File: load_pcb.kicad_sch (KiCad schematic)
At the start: 32 parts, among them J1 Conn_01x16, J2 Conn_01x08, J3 Conn_01x10, P1 282837-2, P2 282837-2, P3 282837-2, P4 282837-2, Q1 BC846BPDW1, Q2 IRFP064V, Q3 IRFP064V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

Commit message: Changed positions of connectors
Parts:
- R14, R15, R16, R17: footprint Resistor_SMD:R_MiniMELF_MMA-0204 -> Resistor_THT:R_Axial_DIN0207_L6.3mm_D2.5mm_P10.16mm_Horizontal
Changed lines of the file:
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@@
       (effects (font (size 1.27 1.27)) (justify left))
     )
-    (property "Footprint" "Resistor_SMD:R_MiniMELF_MMA-0204" (id 2) (at 236.982 77.47 90)
+    (property "Footprint" "Resistor_THT:R_Axial_DIN0207_L6.3mm_D2.5mm_P10.16mm_Horizontal" (id 2) (at 236.982 77.47 90)
       (effects (font (size 1.27 1.27)) hide)
     )
@@
       (effects (font (size 1.27 1.27)) (justify left))
     )
-    (property "Footprint" "Resistor_SMD:R_MiniMELF_MMA-0204" (id 2) (at 248.412 121.92 90)
+    (property "Footprint" "Resistor_THT:R_Axial_DIN0207_L6.3mm_D2.5mm_P10.16mm_Horizontal" (id 2) (at 248.412 121.92 90)
       (effects (font (size 1.27 1.27)) hide)
     )
@@
       (effects (font (size 1.27 1.27)) (justify left))
     )
-    (property "Footprint" "Resistor_SMD:R_MiniMELF_MMA-0204" (id 2) (at 236.982 90.17 90)
+    (property "Footprint" "Resistor_THT:R_Axial_DIN0207_L6.3mm_D2.5mm_P10.16mm_Horizontal" (id 2) (at 236.982 90.17 90)
       (effects (font (size 1.27 1.27)) hide)
     )
@@
       (effects (font (size 1.27 1.27)) (justify left))
     )
-    (property "Footprint" "Resistor_SMD:R_MiniMELF_MMA-0204" (id 2) (at 248.412 109.22 90)
+    (property "Footprint" "Resistor_THT:R_Axial_DIN0207_L6.3mm_D2.5mm_P10.16mm_Horizontal" (id 2) (at 248.412 109.22 90)
       (effects (font (size 1.27 1.27)) hide)
     )
@@
     )
     (path "/4ef2169a-f28b-4852-977e-0f0ba8408b95"
-      (reference "R14") (unit 1) (value "62k") (footprint "Resistor_SMD:R_MiniMELF_MMA-0204")
+      (reference "R14") (unit 1) (value "62k") (footprint "Resistor_THT:R_Axial_DIN0207_L6.3mm_D2.5mm_P10.16mm_Horizontal")
     )
     (path "/809e2eb5-7286-4453-bbbc-874b30752de5"
-      (reference "R15") (unit 1) (value "62k") (footprint "Resistor_SMD:R_MiniMELF_MMA-0204")
+      (reference "R15") (unit 1) (value "62k") (footprint "Resistor_THT:R_Axial_DIN0207_L6.3mm_D2.5mm_P10.16mm_Horizontal")
     )
     (path "/87e237c7-673a-475b-aae1-645c481bc5fe"
-      (reference "R16") (unit 1) (value "62k") (footprint "Resistor_SMD:R_MiniMELF_MMA-0204")
+      (reference "R16") (unit 1) (value "62k") (footprint "Resistor_THT:R_Axial_DIN0207_L6.3mm_D2.5mm_P10.16mm_Horizontal")
     )
     (path "/5b2c9207-c2da-4144-981f-da5833109a74"
-      (reference "R17") (unit 1) (value "62k") (footprint "Resistor_SMD:R_MiniMELF_MMA-0204")
+      (reference "R17") (unit 1) (value "62k") (footprint "Resistor_THT:R_Axial_DIN0207_L6.3mm_D2.5mm_P10.16mm_Horizontal")
     )
     (path "/08372d8d-6e01-436e-bce7-15647a9603ce"

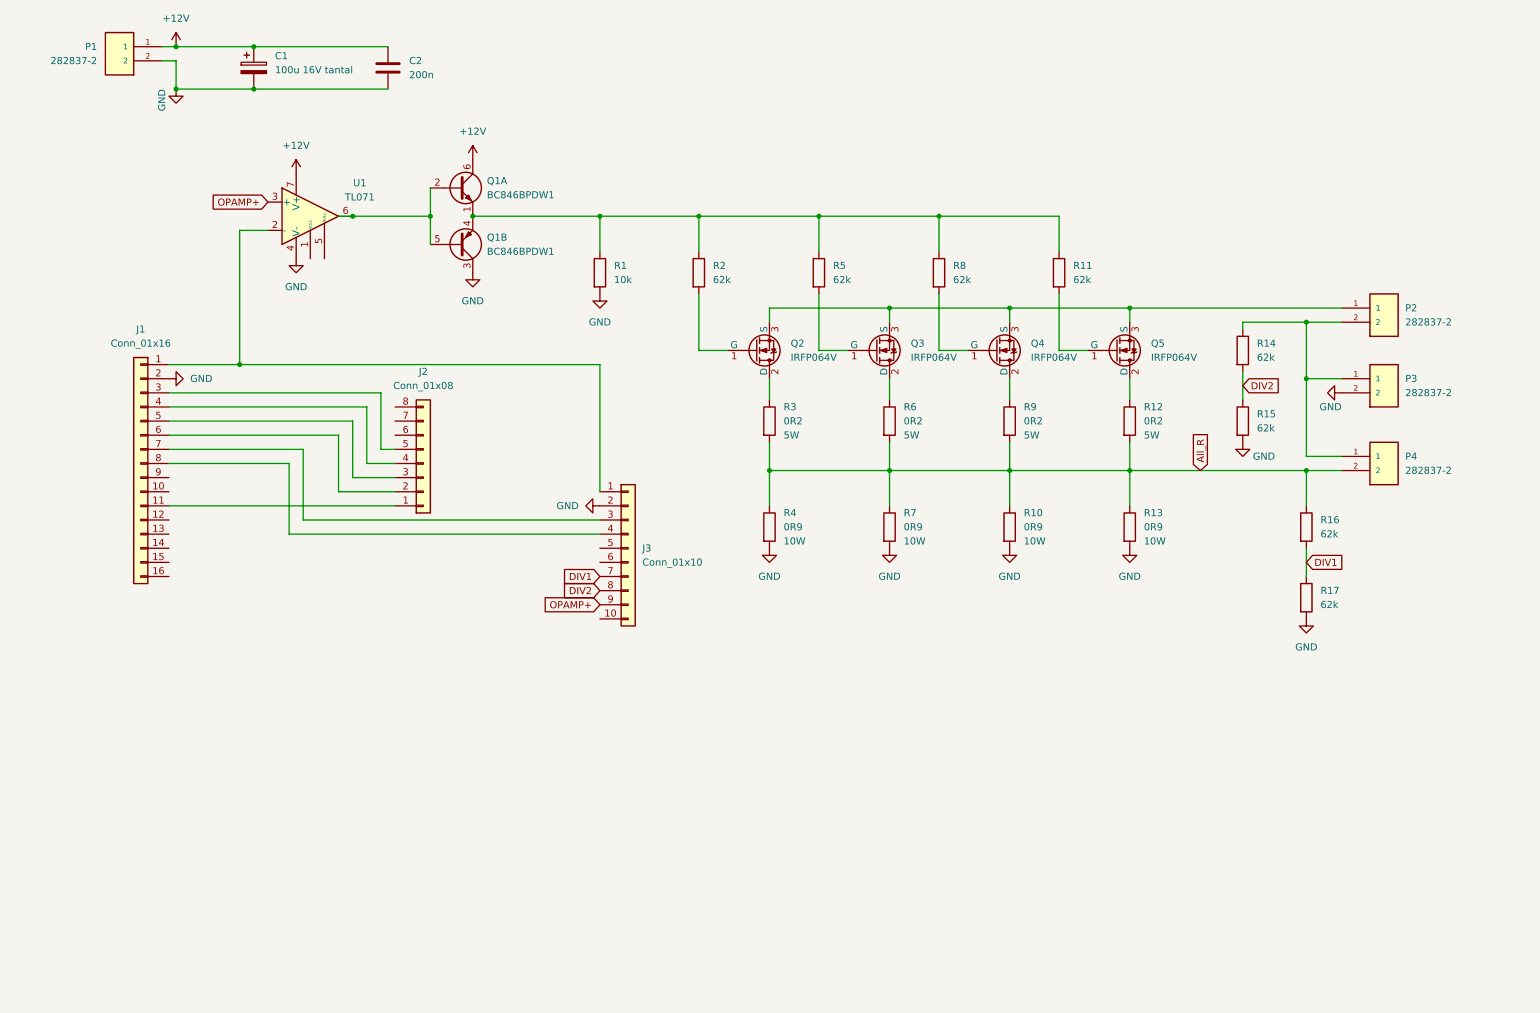
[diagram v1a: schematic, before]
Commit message: Added DAC and corrected positions of SMD/THD
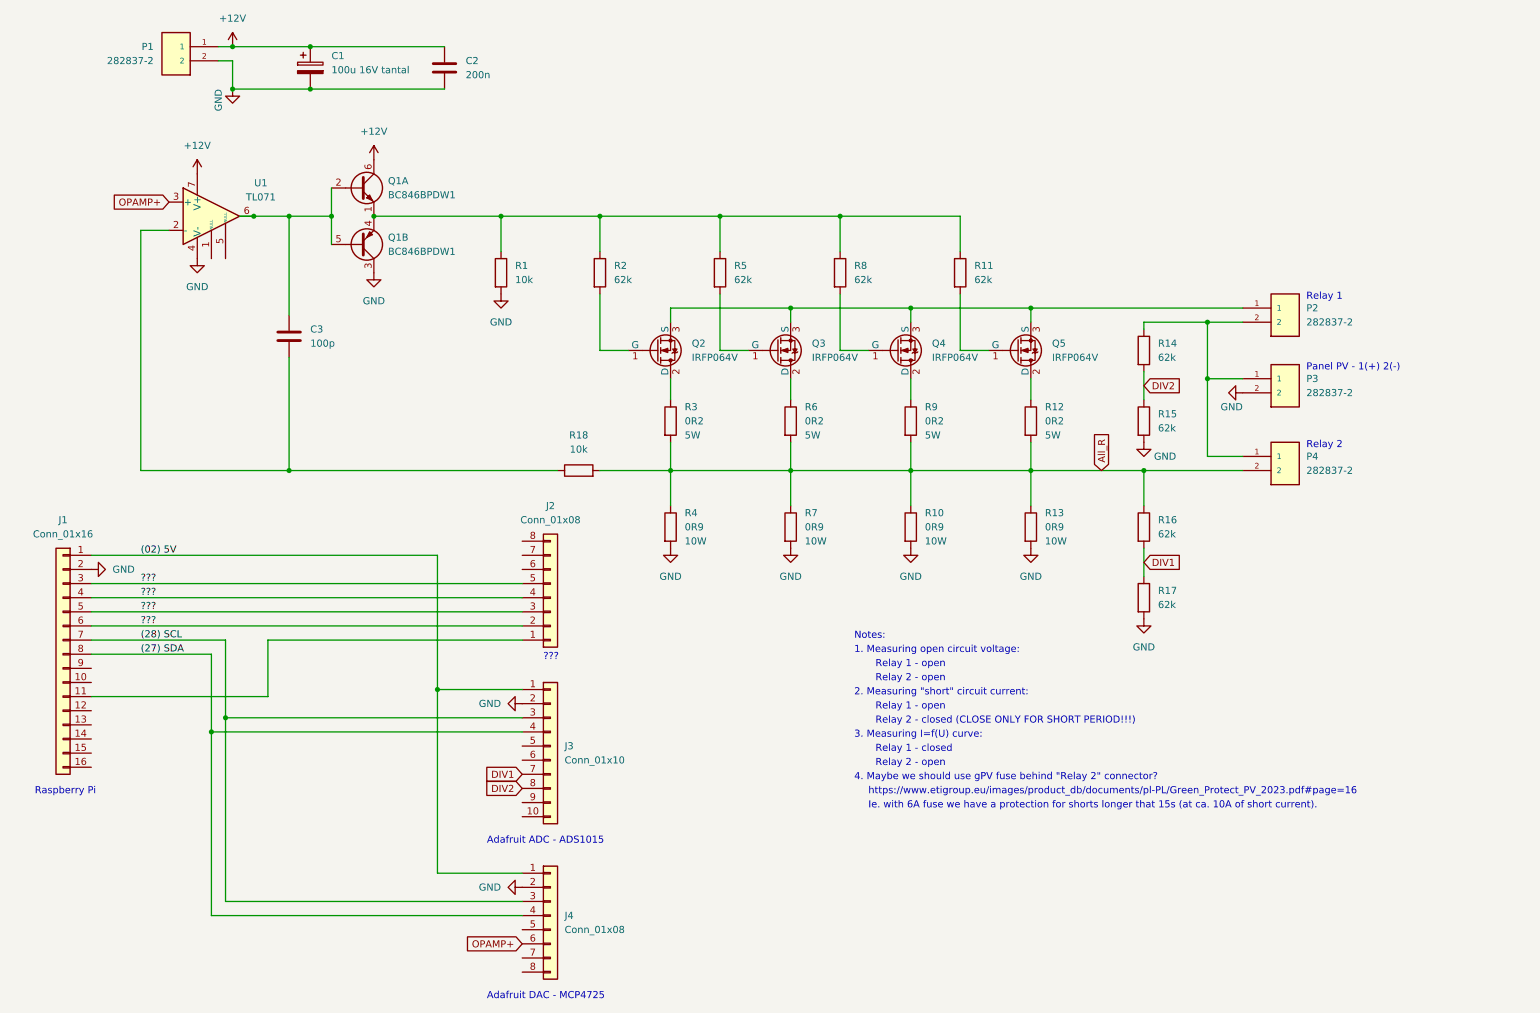
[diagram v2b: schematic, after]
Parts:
- added C3: 100p, Capacitor_SMD:C_1206_3216Metric_Pad1.33x1.80mm_HandSolder, symbol Device:C
- added J4: Conn_01x08, Connector_PinSocket_2.54mm:PinSocket_1x08_P2.54mm_Vertical, symbol Connector_Generic:Conn_01x08
- added R18: 10k, Resistor_SMD:R_1206_3216Metric_Pad1.30x1.75mm_HandSolder, symbol Device:R
- R1, R11, R2, R5, R8: footprint Resistor_SMD:R_MiniMELF_MMA-0204 -> Resistor_SMD:R_1206_3216Metric_Pad1.30x1.75mm_HandSolder
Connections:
- net All_R: now also R18.2
- net GND: now also J4.2 (Pin_2)
- net OPAMP+: now also J4.6 (Pin_6); no longer J3.9 (Pin_9)
- net (02) 5V: now reaches J1.1 (Pin_1), J3.1 (Pin_1)
- net (02) 5V: now also J4.1 (Pin_1); no longer U1.2 (-)
- net at Q1.2 (B1), Q1.5 (B2), U1.6: now also C3.1
- net ???: now reaches J1.3 (Pin_3), J2.5 (Pin_5)
- net ???: now also J1.4 (Pin_4), J1.5 (Pin_5), J1.6 (Pin_6), J2.2 (Pin_2), J2.3 (Pin_3), J2.4 (Pin_4)
- net (28) SCL: now reaches J1.7 (Pin_7), J3.3 (Pin_3)
- net (28) SCL: now also J4.3 (Pin_3)
- net (27) SDA: now reaches J1.8 (Pin_8), J3.4 (Pin_4)
- net (27) SDA: now also J4.4 (Pin_4)
- new net: C3.2, R18.1, U1.2 (-)
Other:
- note added: "1. Measuring open circuit voltage:"
- note added: "2. Measuring "short" circuit current:"
- note added: "3. Measuring I=f(U) curve:"
- note added: "4. Maybe we should use gPV fuse behind "Relay 2" connector?"
- note added: "???"
- note added: "Adafruit ADC - ADS1015"
- note added: "Adafruit DAC - MCP4725"
- note added: "Ie. with 6A fuse we have a protection for shorts longer that 15s (at ca. 10A of short current)."
- note added: "Notes:"
- note added: "Panel PV - 1(+) 2(-)"
- note added: "Raspberry Pi"
- note added: "Relay 1"
- note added: "Relay 1 - closed"
- note added: "Relay 1 - open"
- note added: "Relay 2"
- note added: "Relay 2 - closed (CLOSE ONLY FOR SHORT PERIOD!!!)"
- note added: "Relay 2 - open"
- note added: "https://www.etigroup.eu/images/product_db/documents/pl-PL/Green_Protect_PV_2023.pdf#page=16"
- moved on the sheet: C1, C2, J1, J2, J3, P1, P2, P3, P4, Q1A, Q1B, Q2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

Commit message: Small changes
Corrected values of resistors in voltage dividers and added overvoltage protection for ADC inputs.
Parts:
- added D1, D2: 1N4733A, Diode_THT:D_DO-41_SOD81_P3.81mm_Vertical_AnodeUp, symbol Device:D_Zener
- added R19, R20: 100 1W, Resistor_THT:R_Axial_DIN0309_L9.0mm_D3.2mm_P15.24mm_Horizontal, symbol Device:R
- R14: value 62k -> 9k1
- R15: value 62k -> 1k
- R16: value 62k -> 6k6
- R17: value 62k -> 3k3
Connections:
- net DIV1: now also R19.1
- net DIV2: now also R20.1
- net GND: now also D1.2 (A), D2.2 (A)
- new net: D1.1 (K), R19.2
- new net: D2.1 (K), R20.2
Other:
- note added: "5. Voltage dividers:"
- note added: "Connections between devices"
- note added: "DIV1 max 16.7A input => 5V output"
- note added: "DIV2 max 50V input => 4,95V output"
- note added: "Main circuit"
- note added: "Max voltage of ADC input is VDC + 0.3V = 5.3V"
- note added: "Min voltage of ADC input is -0.3V"
- note added: "Overvoltage protection for ADC"
- note added: "Pmax=22.7mW (I=16.7A)"
- note added: "Pmax=227mW (U=50V)"
- note added: "Power supply cap filter"
- moved on the sheet: C1, C2, C3, P1, P2, P3, P4, Q1A, Q1B, Q2, Q3, Q4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

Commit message: Add a simulation in LTspice and production files
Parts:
- removed U1: TL071, Package_DIP:DIP-8_W7.62mm_Socket, symbol Amplifier_Operational:TL071
- added F1: 10A gPV, proj_lib:Fuse_gPV_10.3x38mm, symbol Device:Fuse
- added R21: 36k, Resistor_THT:R_Axial_DIN0207_L6.3mm_D2.5mm_P10.16mm_Horizontal, symbol Device:R
- added U1: LM358, Package_DIP:DIP-8_W7.62mm_Socket_LongPads, symbol Amplifier_Operational:LM358
- C2: value 200n -> 100n
- R1: footprint Resistor_SMD:R_1206_3216Metric_Pad1.30x1.75mm_HandSolder -> Resistor_THT:R_Axial_DIN0207_L6.3mm_D2.5mm_P10.16mm_Horizontal
- R11, R2, R5, R8: value 62k -> 6k2; footprint Resistor_SMD:R_1206_3216Metric_Pad1.30x1.75mm_HandSolder -> Resistor_THT:R_Axial_DIN0207_L6.3mm_D2.5mm_P10.16mm_Horizontal
- R18: value 10k -> 1k; footprint Resistor_SMD:R_1206_3216Metric_Pad1.30x1.75mm_HandSolder -> Resistor_THT:R_Axial_DIN0207_L6.3mm_D2.5mm_P10.16mm_Horizontal
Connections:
- net +12V: now also U1.8 (V+)
- net GND: now also U1.4 (V-), U1.5 (+), U1.6 (-)
- net OPAMP+: now also U1.3 (+)
- net at C3.2, R18.1: now also R21.1, U1.2 (-)
- net at C3.1, Q1.2 (B1), Q1.5 (B2): now also R21.2, U1.1
- net at P2.2, P4.1, R14.1: now also F1.1; no longer P3.1
- new net: F1.2, P3.1
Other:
- moved on the sheet: C3, P3
